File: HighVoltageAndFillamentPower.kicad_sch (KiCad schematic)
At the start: 12 parts, among them Q16 410N, T1 Wuerth_750315371

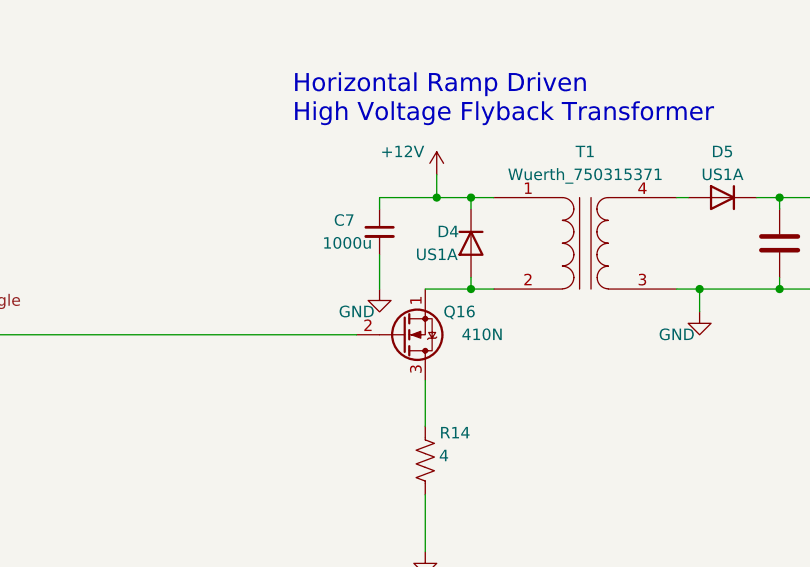
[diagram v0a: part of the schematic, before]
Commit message: linked models so spice simulation runs
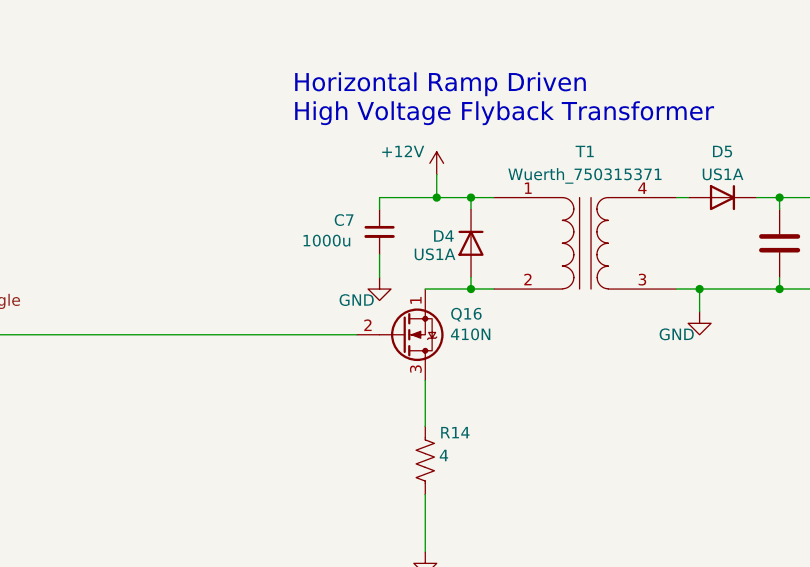
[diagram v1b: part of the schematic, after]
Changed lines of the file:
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@@
 	(wire
 		(pts
-			(xy 121.92 86.36) (xy 121.92 90.17)
+			(xy 121.92 86.36) (xy 121.92 88.9)
 		)
 		(stroke
@@
 	(symbol
 		(lib_id "power:GND")
-		(at 121.92 90.17 0)
+		(at 121.92 88.9 0)
 		(unit 1)
 		(exclude_from_sim no)
@@
 		(dnp no)
 		(property "Reference" "#PWR09"
-			(at 121.92 96.52 0)
+			(at 121.92 95.25 0)
 			(effects
 				(font
@@
 		)
 		(property "Value" "GND"
-			(at 119.38 92.71 0)
+			(at 119.38 91.44 0)
 			(effects
 				(font
@@
 		)
 		(property "Footprint" ""
-			(at 121.92 90.17 0)
+			(at 121.92 88.9 0)
 			(effects
 				(font
@@
 		)
 		(property "Datasheet" ""
-			(at 121.92 90.17 0)
+			(at 121.92 88.9 0)
 			(effects
 				(font
@@
 		)
 		(property "Description" ""
-			(at 121.92 90.17 0)
+			(at 121.92 88.9 0)
 			(effects
 				(font
@@
 		)
 		(property "Sim.Device" "V"
-			(at 121.92 90.17 0)
+			(at 121.92 88.9 0)
 			(effects
 				(font
@@
 		)
 		(property "Sim.Type" "DC"
-			(at 121.92 90.17 0)
+			(at 121.92 88.9 0)
 			(effects
 				(font
@@
 		)
 		(property "Sim.Pins" "1=+"
-			(at 121.92 90.17 0)
+			(at 121.92 88.9 0)
 			(effects
 				(font
@@
 		)
 		(property "Sim.Params" "dc=0"
-			(at 121.92 90.17 0)
+			(at 121.92 88.9 0)
 			(effects
 				(font
@@
 		(dnp no)
 		(property "Reference" "D4"
-			(at 129.54 83.82 90)
+			(at 129.032 84.328 90)
 			(effects
 				(font
@@
 		)
 		(property "Value" "US1A"
-			(at 128.27 86.36 90)
+			(at 128.016 86.36 90)
 			(effects
 				(font
@@
 		)
 		(property "Value" "1000u"
-			(at 115.57 85.09 0)
+			(at 113.284 84.836 0)
 			(effects
 				(font
@@
 		(dnp no)
 		(property "Reference" "Q16"
-			(at 130.81 92.71 0)
+			(at 131.572 92.964 0)
 			(effects
 				(font
@@
 		)
 		(property "Value" "410N"
-			(at 133.35 95.25 0)
-			(effects
-				(font
+			(at 132.08 95.25 0)
+			(effects
+				(font

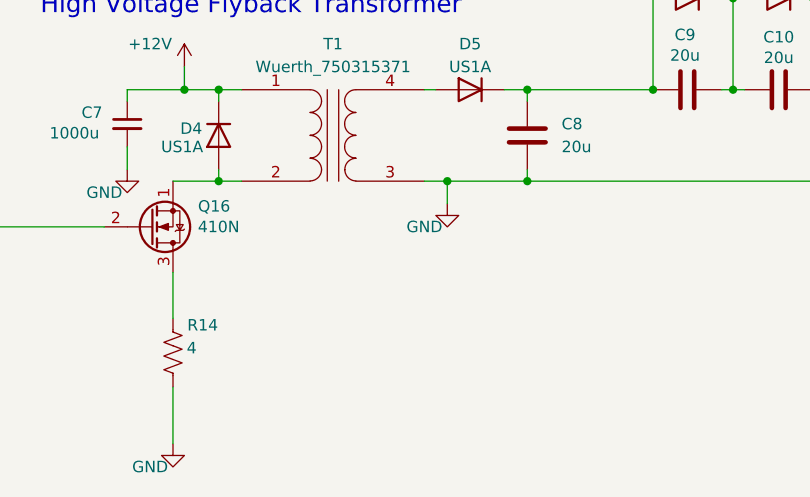
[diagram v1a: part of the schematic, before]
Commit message: added sections to add to overview schematic, added some of the component schematics
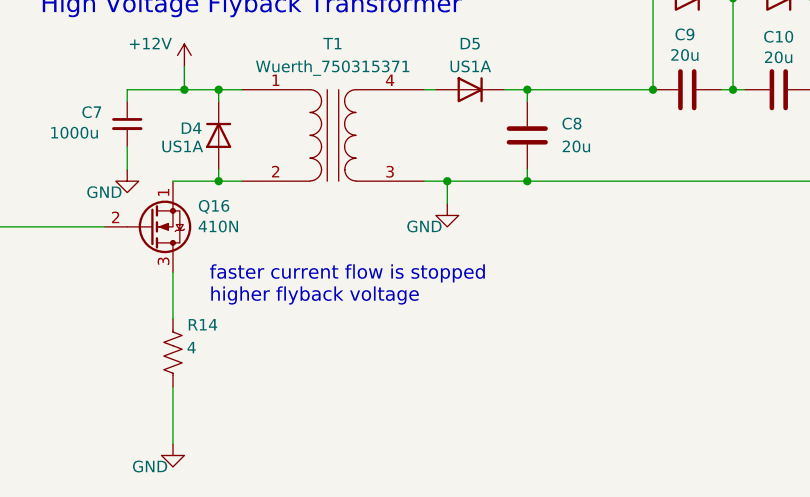
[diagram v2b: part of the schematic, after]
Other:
- note added: "faster current flow is stopped higher flyback voltage"
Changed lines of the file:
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@@
+		)
+	)
+	(text "faster current flow is stopped\nhigher flyback voltage"
+		(exclude_from_sim no)
+		(at 131.064 103.886 0)
+		(effects
+			(font
+				(size 1.524 1.524)
+			)
+			(justify left bottom)
 		)
 	)
@@
 		(shape input)
 		(at 67.31 91.44 0)
-		(fields_autoplaced yes)
 		(effects
 			(font
